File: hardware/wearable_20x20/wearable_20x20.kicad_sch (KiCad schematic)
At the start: 0 parts

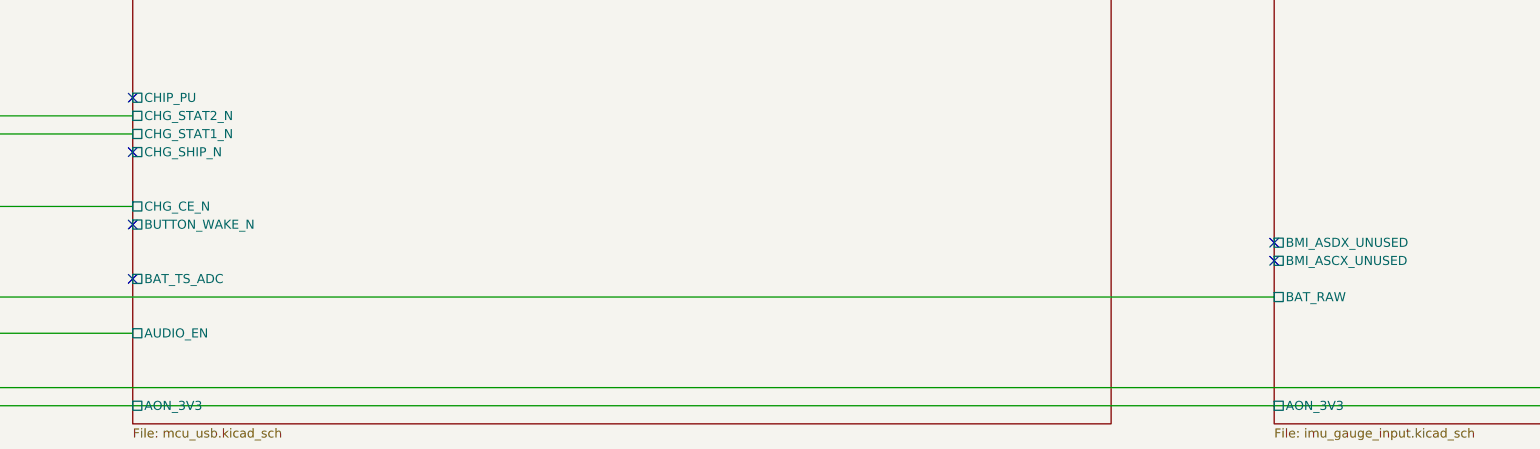
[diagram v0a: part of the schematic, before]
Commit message: Regenerate hierarchies with selected EVT parts
Co-authored-by: illiapliukhin <illiapliukhin@users.noreply.github.com>
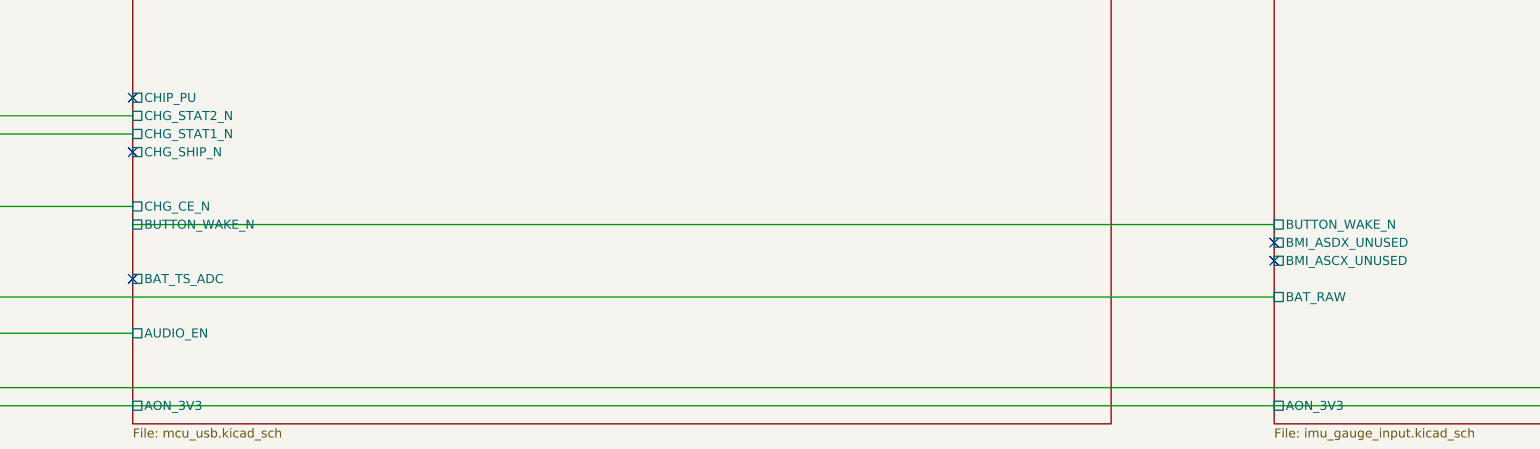
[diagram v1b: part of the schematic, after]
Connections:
- no-connect marks 102 -> 101
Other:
- sheet IMU_Gauge_Input ports: added BUTTON_WAKE_N; removed none
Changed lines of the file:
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@@
-	)
-	(no_connect
-		(at 180.34 541.02)
 	)
 	(no_connect
@@
 		(pts
 			(xy 180.34 254) (xy 340.36 254)
+		)
+		(stroke
+			(width 0)
+			(type default)
+		)
+	)
+	(wire
+		(pts
+			(xy 180.34 541.02) (xy 340.36 541.02)
 		)
 		(stroke
@@
 			(effects
 				(font
+					(size 1.27 1.27)
+				)
+				(justify left)
+			)
+		)
+		(pin "BUTTON_WAKE_N" passive
+			(at 340.36 541.02 180)
+			(effects
+				(font
